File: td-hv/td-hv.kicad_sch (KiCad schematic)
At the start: 47 parts, among them J1 Conn_01x07_Male, Q1 IMBF170R450M1XTMA1, U1 UCC2801, U2 TLC272, U3 LM2903

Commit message: finish layout
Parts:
- removed L2: L, Inductor_SMD:L_Bourns_SRR1260, symbol Device:L
- removed R15: R, Resistor_THT:R_Radial_Power_L13.0mm_W9.0mm_P5.00mm, symbol Device:R
- removed RV2: 10k, Potentiometer_SMD:Potentiometer_Bourns_3314G_Vertical, symbol Device:R_POT_TRIM
- removed U1: UCC2801, Package_SO:SOIC-8_3.9x4.9mm_P1.27mm, symbol Regulator_Controller:UCC3801
- added C13: 0.001uF, Capacitor_SMD:C_0805_2012Metric, symbol Device:C
- added C14: 0.1uF, Capacitor_SMD:C_0805_2012Metric, symbol Device:C
- added D4, D5: GREEN, LED_SMD:LED_0805_2012Metric, symbol Device:LED
- added R18: 10, Resistor_SMD:R_0805_2012Metric, symbol Device:R
- added R19, R20, R22: 100k, Resistor_SMD:R_0805_2012Metric, symbol Device:R
- added R21: 10k, Resistor_SMD:R_0805_2012Metric, symbol Device:R
- added RV2: 1k, Potentiometer_SMD:Potentiometer_Bourns_3314G_Vertical, symbol Device:R_Potentiometer_Trim
- added U1: UCC35701, Package_SO:SOIC-14_3.9x8.7mm_P1.27mm, symbol td-hv:UCC35701
- C1, C11: value 10000pF -> 0.1uF; Digikey 732-12139-1-ND -> 478-10836-1-ND
- C10, C8, C9: Digikey (none) -> 478-10836-1-ND
- C12: value 0.01uF -> 0.001uF; Digikey (none) -> 311-1122-1-ND
- C3: value 560pF -> 0.1uF; Digikey 399-1134-1-ND -> 478-10836-1-ND
- C4: value 12uF 250V -> 6.8uF 200V; symbol Device:CP -> Device:C_Polarized; Digikey 493-6735-1-ND -> 493-9979-1-ND
- D2: value ‎150080GS75000‎ -> GREEN
- D3: value LED -> RED; Digikey 732-4984-1-ND -> 350-2039-1-ND
- E1: symbol Device:SPARK_GAP -> Device:SparkGap; Digikey (none) -> 2087-150-SM-RPLFCT-ND
- J1: Digikey 455-2238-ND -> 1175-51025-07-0100-01-ND
- Q1: Digikey 448-IMBF170R450M1XTMA1CT-ND -> 448-IMBG120R220M1HXTMA1CT-ND
- R10: Digikey 13-RC2512JK-073KLCT-ND‎ -> 13-RC2512FK-073KLCT-ND
- R11: value 120 -> 39k; Digikey (none) -> 311-39.0KCRCT-ND
- R12: value 50 -> 10k; Digikey (none) -> 311-10.0KCRCT-ND
- R13: value 1k -> 1.4k; Digikey (none) -> 311-1.40KCRCT-ND
- R14, R16, R17: Digikey (none) -> 311-10.0KCRCT-ND
- R3: value 1 -> 1M; Digikey YAG3705CT-ND -> 311-1.00MCRCT-ND
- RV1: symbol Device:R_POT_TRIM -> Device:R_Potentiometer_Trim
- U2: Digikey (none) -> 296-7204-5-ND
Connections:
- net +12V: now also R21.1, U1.3 (VDD); no longer R13.1
- net GND: now also C1.2, C3.1, R13.1, R2.2, R3.2, C13.2, D4.1 (K), D5.1 (K), R20.2, RV2.1, U1.13 (GND), U1.5 (PNGD); no longer C12.2, R5.2
- net VBUS: now also L1.2, R10.1, R22.1
- net fb: now also C11.1, C12.1, U1.8 (FB); no longer R14.2, U2.2 (-)
- net sync_in: now also U1.11 (SYNC); no longer R11.2
- net at L1.7: now also R5.1, R19.1
- net at Q1.1 (G): now also R18.2; no longer R3.1
- net at R1.2: now also R2.1, U1.9 (VSCLAMP); no longer C1.2
- net at R13.2: now also U1.7 (RT); no longer C8.1
- net at U2.3 (+): now also RV2.2; no longer R5.1
- net at C11.2: now also R14.1; no longer R1.1
- net at RV1.2, U3.2 (-): now also U3.6 (_); no longer U3.5 (+)
- net comp renamed ss
- net ss: now also U1.14 (SS); no longer C11.1, R14.1
- net cs: no longer names the net of R17.2
- net cs: now also C13.1, U1.2 (ILIM); no longer C12.1
- removed net ucc3801_ref: C2.1, R2.2, U3.3 (+), U3.6 (_)
- new net: C12.2, C14.2, R14.2, R20.1, R5.2, U2.2 (-)
- new net: C2.1, R3.1, U1.1 (COUNT)
- new net: C3.2, U1.10 (CT)
- new net: R18.1, U1.4 (OUT)
- new net: R11.2, R12.1, U1.6 (VFF)
- new net: D4.2 (A), R21.2
- new net: C14.1, R19.2
- new net: D5.2 (A), R22.2
- new net +5V: C8.1, R1.1, R11.1, RV2.3, U1.12 (VREF), U3.3 (+), U3.5 (+)
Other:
- note added: "todo: make x-ray protect actually shut down"
- note added: "type III compensation optional"
- note removed: "turn-on damping"
- moved on the sheet: C9, U2A, U2C

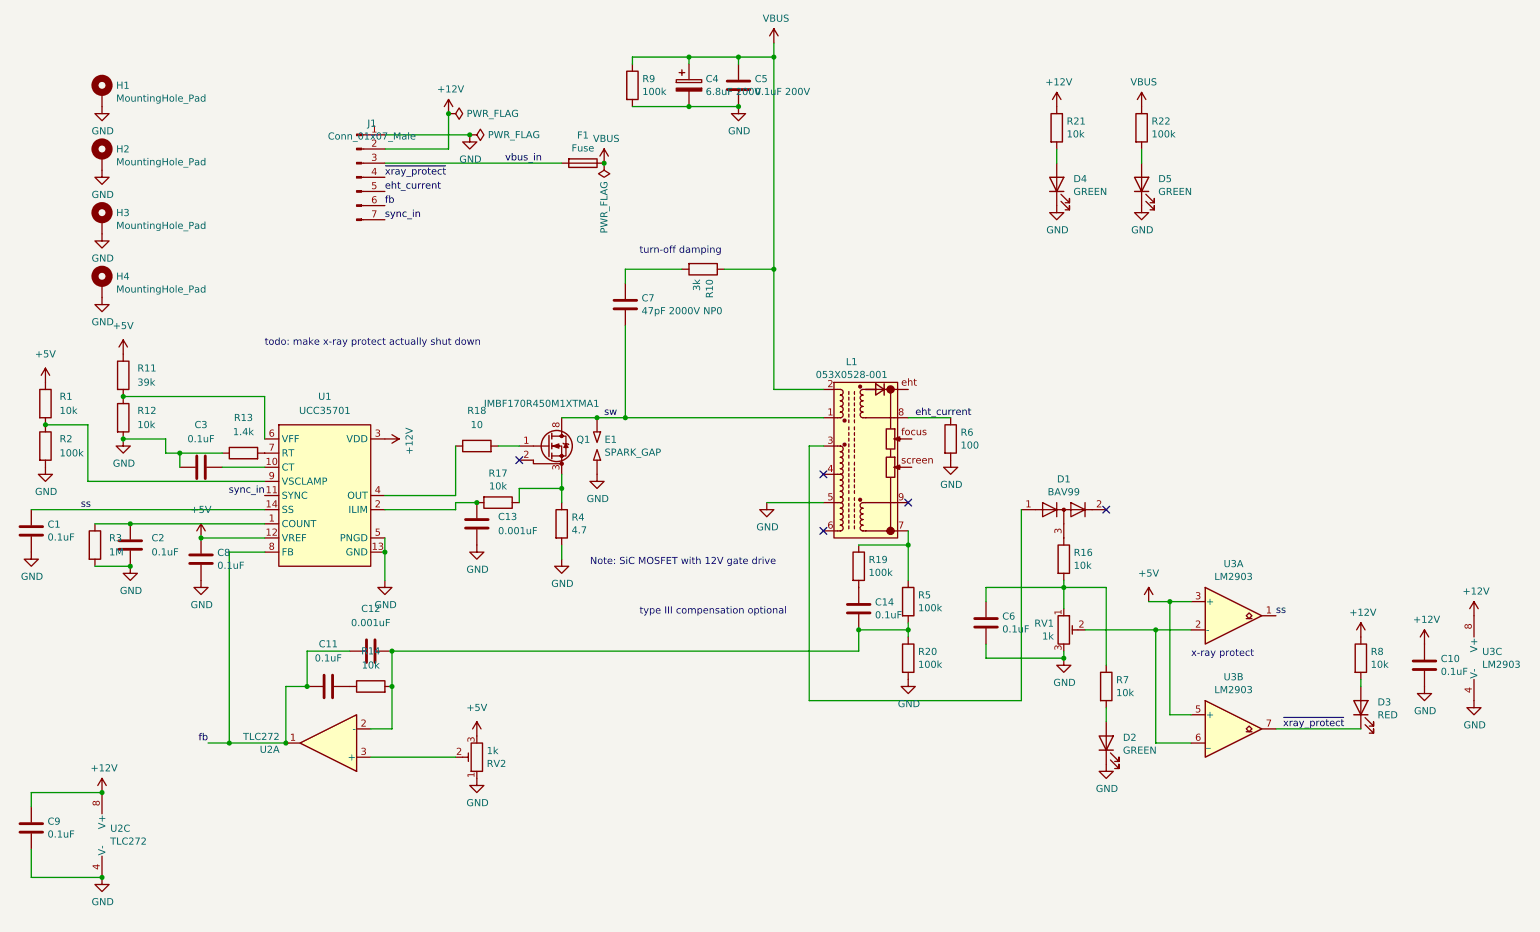
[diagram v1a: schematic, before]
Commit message: update td-hv schematic to match currently built circuit
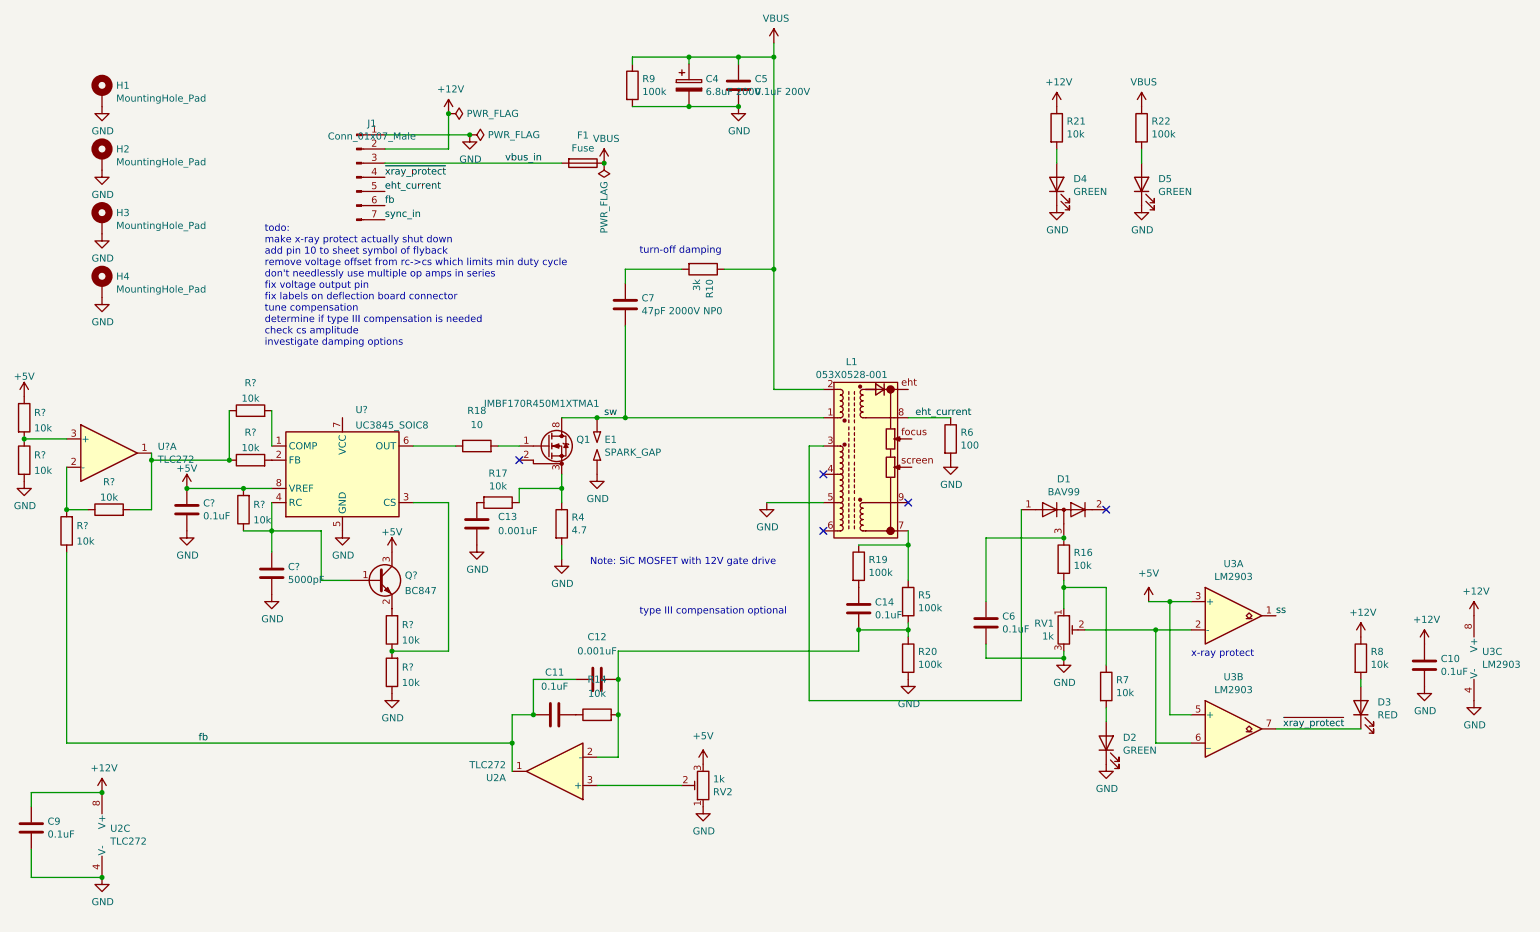
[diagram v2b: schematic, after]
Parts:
- removed C1, C2, C3, C8: 0.1uF, Capacitor_SMD:C_0805_2012Metric, symbol Device:C
- removed R1, R12: 10k, Resistor_SMD:R_0805_2012Metric, symbol Device:R
- removed R11: 39k, Resistor_SMD:R_0805_2012Metric, symbol Device:R
- removed R13: 1.4k, Resistor_SMD:R_0805_2012Metric, symbol Device:R
- removed R2: 100k, Resistor_SMD:R_0805_2012Metric, symbol Device:R
- removed R3: 1M, Resistor_SMD:R_0805_2012Metric, symbol Device:R
- removed U1: UCC35701, Package_SO:SOIC-14_3.9x8.7mm_P1.27mm, symbol td-hv:UCC35701
- added C?: 0.1uF, Capacitor_SMD:C_0805_2012Metric, symbol Device:C
- added C?: 5000pF, Capacitor_SMD:C_0805_2012Metric, symbol Device:C
- added Q?: BC847, Package_TO_SOT_SMD:SOT-23, symbol Transistor_BJT:BC847
- added R? (x9): 10k, symbol Device:R
- added U?: TLC272, Package_SO:SOIC-8_3.9x4.9mm_P1.27mm, symbol Amplifier_Operational:TLC272
- added U?: UC3845_SOIC8, Package_SO:SOIC-8_3.9x4.9mm_P1.27mm, symbol Regulator_Controller:UC3845_SOIC8
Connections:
- net +5V: now also C?.1, Q?.3 (C), R?.1, R?.2, U?.8 (VREF)
- net GND: now also C?.2, C?.2, R?.1, R?.2, U?.5 (GND)
- net fb: now also R?.1
- net at D1.3 (K), R16.1: now also C6.1
- net at R16.2, R7.1, RV1.1: no longer C6.1
- net at R18.1: now also U?.6 (OUT)
- new net: R?.1, R?.1, R?.2, U?.1
- new net: R?.2, U?.1 (COMP)
- new net: C?.1, Q?.1 (B), R?.1, U?.4 (RC)
- new net: Q?.2 (E), R?.2
- new net: R?.1, R?.2, U?.2 (-)
- new net: R?.1, R?.2, U?.3 (+)
- new net: R?.1, R?.2, U?.3 (CS)
- new net: R?.2, U?.2 (FB)
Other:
- note added: "todo: make x-ray protect actually shut down add pin 10 to sheet symbol of flyback remove voltage offset from rc->cs which limits min duty cycle don't needlessly use multiple op amps in series fix voltage output pin fix labels on deflection board connector tune compensation determine if type III compensation is needed check cs amplitude investigate damping options"
- note removed: "todo: make x-ray protect actually shut down"
- moved on the sheet: C11, C12, R14, RV2, U2A

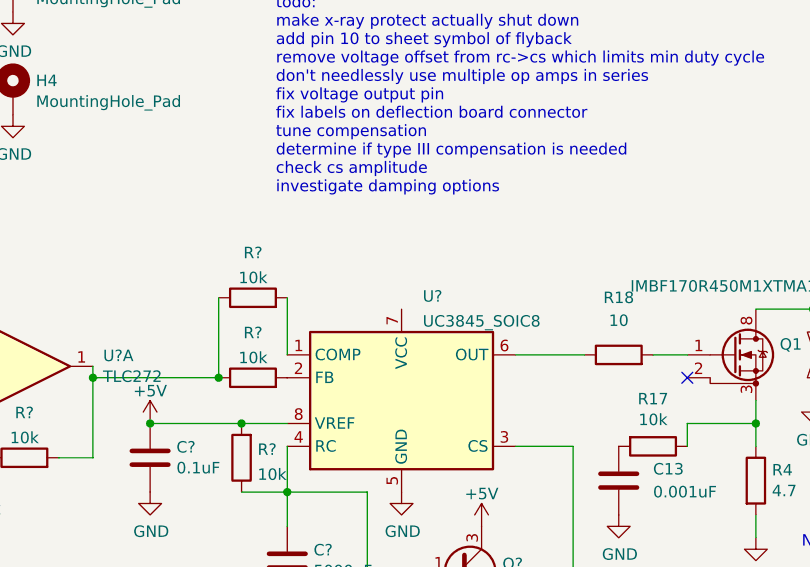
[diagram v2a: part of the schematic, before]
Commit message: attach vcc to the 3845
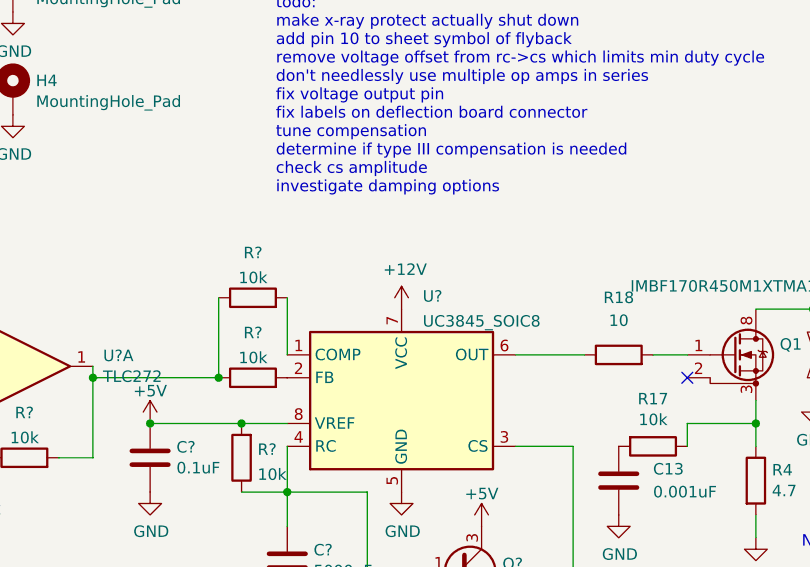
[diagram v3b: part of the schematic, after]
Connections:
- net +12V: now also U?.7 (VCC)
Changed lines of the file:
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@@
+    (pin "1")
+  )
+  (symbol (lib_id "power:+12V") (at 74.93 85.09 0) (unit 1)
+    (in_bom yes) (on_board yes)
+    (property "Reference" "#PWR?" (id 0) (at 74.93 88.9 0)
+      (effects (font (size 1.27 1.27)) hide)
+    )
+    (property "Value" "+12V" (id 1) (at 75.311 80.6958 0))
+    (property "Footprint" "" (id 2) (at 74.93 85.09 0)
+      (effects (font (size 1.27 1.27)) hide)
+    )
+    (property "Datasheet" "" (id 3) (at 74.93 85.09 0)
+      (effects (font (size 1.27 1.27)) hide)
+    )
     (pin "1")
   )
@@
       (reference "#PWR?") (unit 1) (value "GND") (footprint "")
     )
+    (path "/a230ab96-5008-4df0-b115-bd681dd2a0fb"
+      (reference "#PWR?") (unit 1) (value "+12V") (footprint "")
+    )
     (path "/a7fce61c-f0e9-47ca-a1ed-f85298b8ea55"

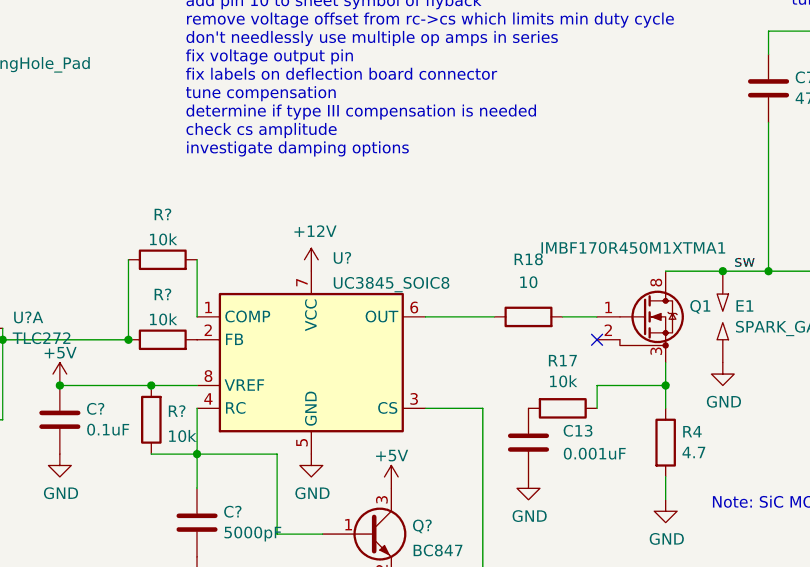
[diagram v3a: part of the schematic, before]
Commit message: change part number of ucc38c45
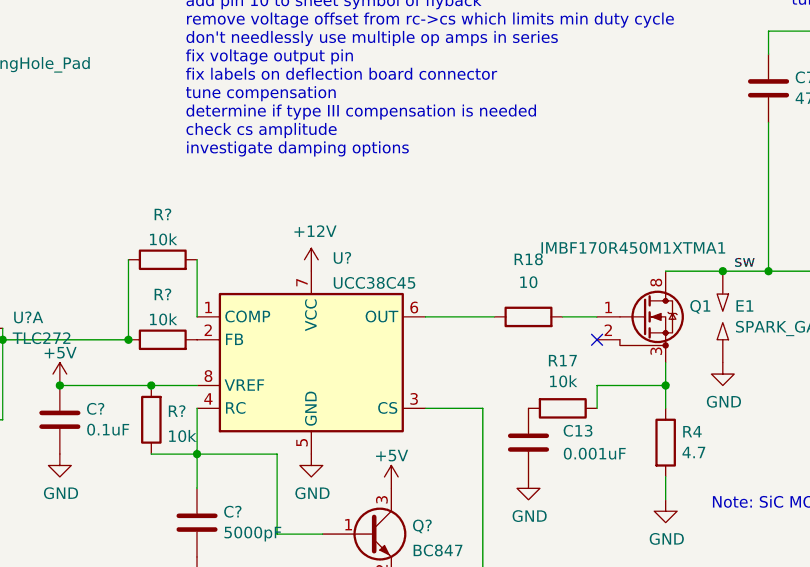
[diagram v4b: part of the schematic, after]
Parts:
- U?: value UC3845_SOIC8 -> UCC38C45
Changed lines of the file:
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@@
       (effects (font (size 1.27 1.27)) (justify left))
     )
-    (property "Value" "UC3845_SOIC8" (id 1) (at 77.2732 86.4386 0)
+    (property "Value" "UCC38C45" (id 1) (at 77.2732 86.4386 0)
       (effects (font (size 1.27 1.27)) (justify left))
     )
@@
     )
     (path "/e54c477d-0eb4-402a-8131-7adb553e251e"
-      (reference "U?") (unit 1) (value "UC3845_SOIC8") (footprint "Package_SO:SOIC-8_3.9x4.9mm_P1.27mm")
-    )
-  )
+      (reference "U?") (unit 1) (value "UCC38C45") (footprint "Package_SO:SOIC-8_3.9x4.9mm_P1.27mm")
+    )
+  )

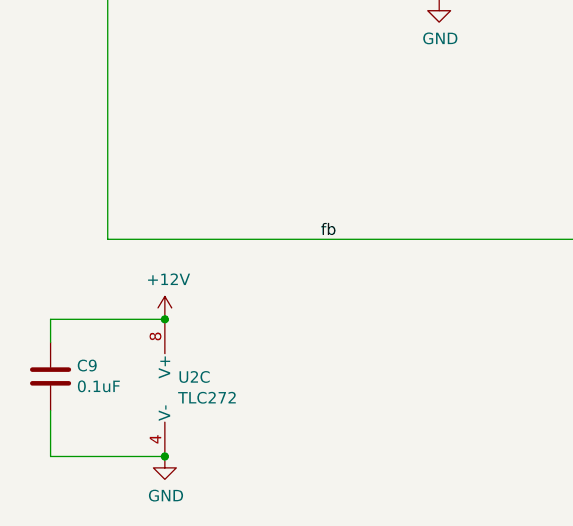
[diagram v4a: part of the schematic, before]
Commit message: switch tlc272 power source to 5v
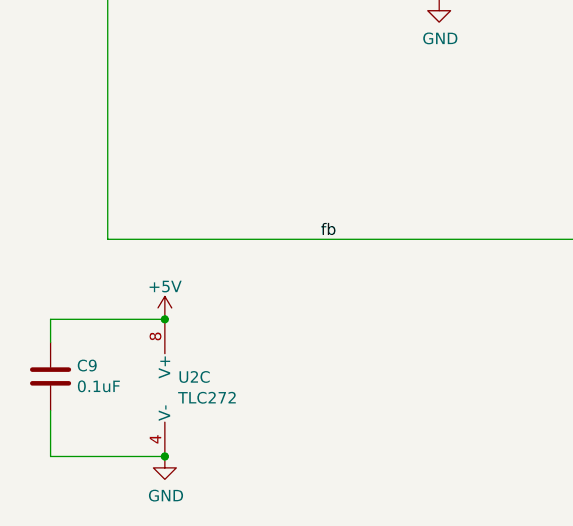
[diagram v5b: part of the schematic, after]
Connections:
- net +12V: no longer C9.1, U2.8 (V+)
- net +5V: now also C9.1, U2.8 (V+)
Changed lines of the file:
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@@
 (kicad_sch (version 20220103) (generator eeschema)
   (paper "A4")
+  (junction (at 31.75 152.4) (diameter 0) (color 0 0 0 0)
+  )
   (junction (at 62.23 105.41) (diameter 0) (color 0 0 0 0)
   )
@@
   )
   (junction (at 93.98 30.48) (diameter 0) (color 0 0 0 0)
-  )
-  (junction (at 31.75 152.4) (diameter 0) (color 0 0 0 0)
   )
   (junction (at 25.4 101.6) (diameter 0) (color 0 0 0 0)
@@
     (pin "2")
   )
-  (symbol (lib_id "power:+12V") (at 31.75 152.4 0) (unit 1)
-    (in_bom yes) (on_board yes)
-    (property "Reference" "#PWR0122" (id 0) (at 31.75 156.21 0)
-      (effects (font (size 1.27 1.27)) hide)
-    )
-    (property "Value" "+12V" (id 1) (at 32.131 148.0058 0))
-    (property "Footprint" "" (id 2) (at 31.75 152.4 0)
-      (effects (font (size 1.27 1.27)) hide)
-    )
-    (property "Datasheet" "" (id 3) (at 31.75 152.4 0)
-      (effects (font (size 1.27 1.27)) hide)
-    )
-    (pin "1")
-  )
   (symbol (lib_id "power:GND") (at 31.75 167.64 0) (unit 1)
     (in_bom yes) (on_board yes)
@@
     )
     (property "Datasheet" "" (id 3) (at 139.7 147.32 0)
+      (effects (font (size 1.27 1.27)) hide)
+    )
+    (pin "1")
+  )
+  (symbol (lib_id "power:+5V") (at 31.75 152.4 0) (unit 1)
+    (in_bom yes) (on_board yes) (fields_autoplaced)
+    (property "Reference" "#PWR?" (id 0) (at 31.75 156.21 0)
+      (effects (font (size 1.27 1.27)) hide)
+    )
+    (property "Value" "+5V" (id 1) (at 31.75 148.7955 0))
+    (property "Footprint" "" (id 2) (at 31.75 152.4 0)
+      (effects (font (size 1.27 1.27)) hide)
+    )
+    (property "Datasheet" "" (id 3) (at 31.75 152.4 0)
       (effects (font (size 1.27 1.27)) hide)
     )
@@
       (reference "#PWR0119") (unit 1) (value "GND") (footprint "")
     )
-    (path "/00000000-0000-0000-0000-000061007dfb"
-      (reference "#PWR0122") (unit 1) (value "+12V") (footprint "")
-    )
     (path "/00000000-0000-0000-0000-00006100804d"
       (reference "#PWR0123") (unit 1) (value "GND") (footprint "")
@@
       (reference "#PWR0130") (unit 1) (value "GND") (footprint "")
     )
+    (path "/4027a2bf-7863-4682-b9d4-79ddef959416"
+      (reference "#PWR?") (unit 1) (value "+5V") (footprint "")
+    )
     (path "/48e40fb7-d693-461f-a944-5b99c4d21ea9"
